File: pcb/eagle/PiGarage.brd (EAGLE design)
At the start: 65 x 30 mm, 19 parts, among them J1 JST_2PIN_HEADER, J2 JST_2PIN_HEADER, J3 JST_2PIN_HEADER, K1 G5LE, T1 NUD3105

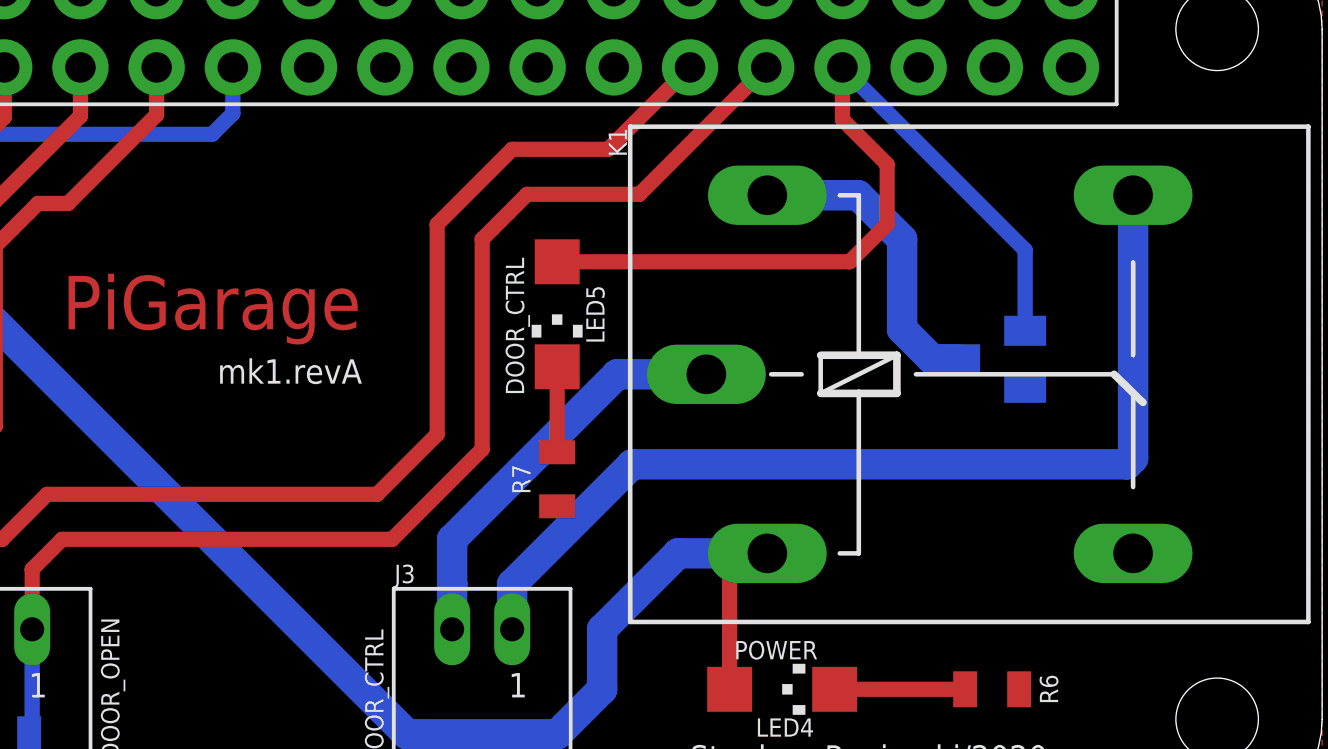
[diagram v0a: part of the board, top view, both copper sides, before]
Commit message: Fixed relay NC/NO pin swap issue, bumped board rev to mk1.revB
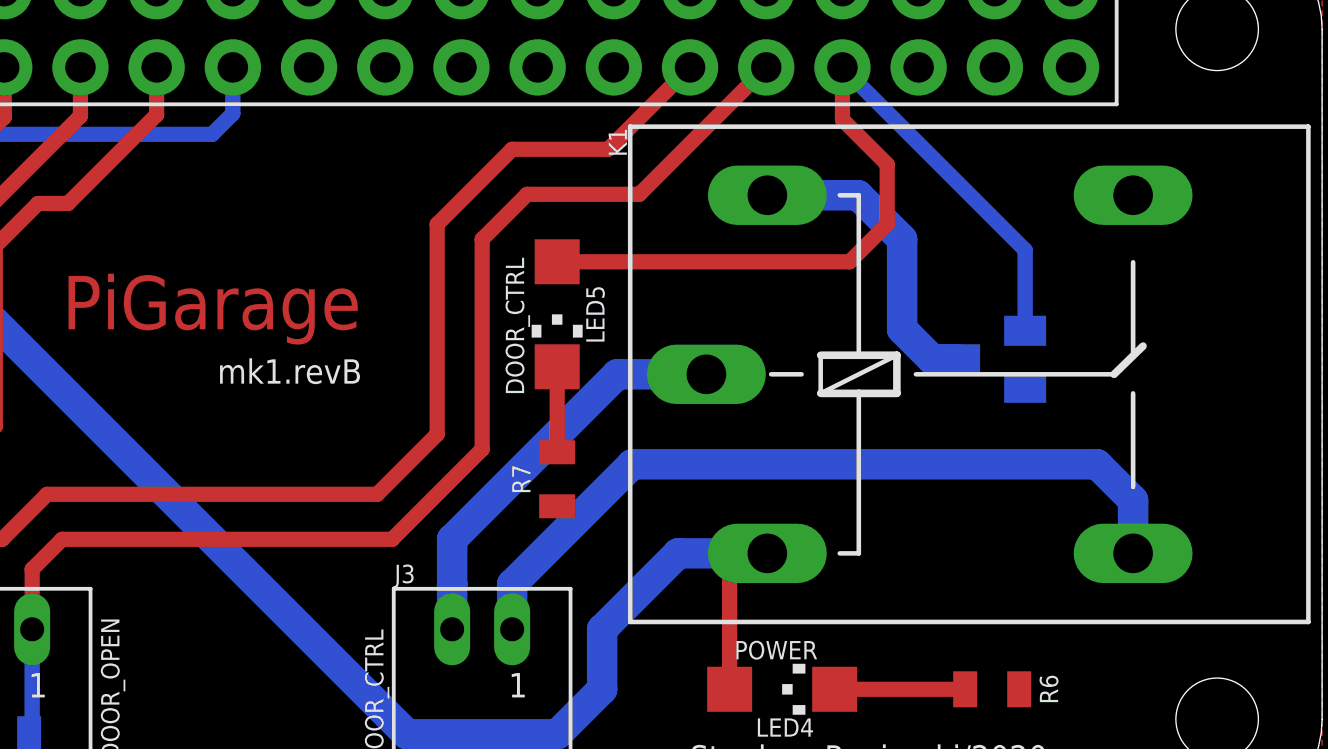
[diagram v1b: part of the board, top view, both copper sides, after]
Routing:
- net N$4: track 32.7 -> 26.1 mm
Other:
- board text added: "mk1.revB"
- board text removed: "mk1.revA"
